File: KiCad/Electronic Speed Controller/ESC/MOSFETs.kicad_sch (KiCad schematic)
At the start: 0 parts

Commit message: Create MOSFETs driver schematic
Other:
- note added: "${TITLE}"
- title: (none) -> MOSFETs
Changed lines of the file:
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@@
 	(paper "A4")
 	(title_block
+		(title "MOSFETs")
 		(date "2025-01-09")
 		(rev "rev_1")
@@
 		(comment 4 "+212 643 241 400")
 	)
+	(text "${TITLE}"
+		(exclude_from_sim no)
+		(at 136.906 22.86 0)
+		(effects
+			(font
+				(face "Cascadia Mono NF")
+				(size 7.62 7.62)
+				(thickness 0.762)
+				(bold yes)
+			)
+			(justify top)
+		)
+	)
 )

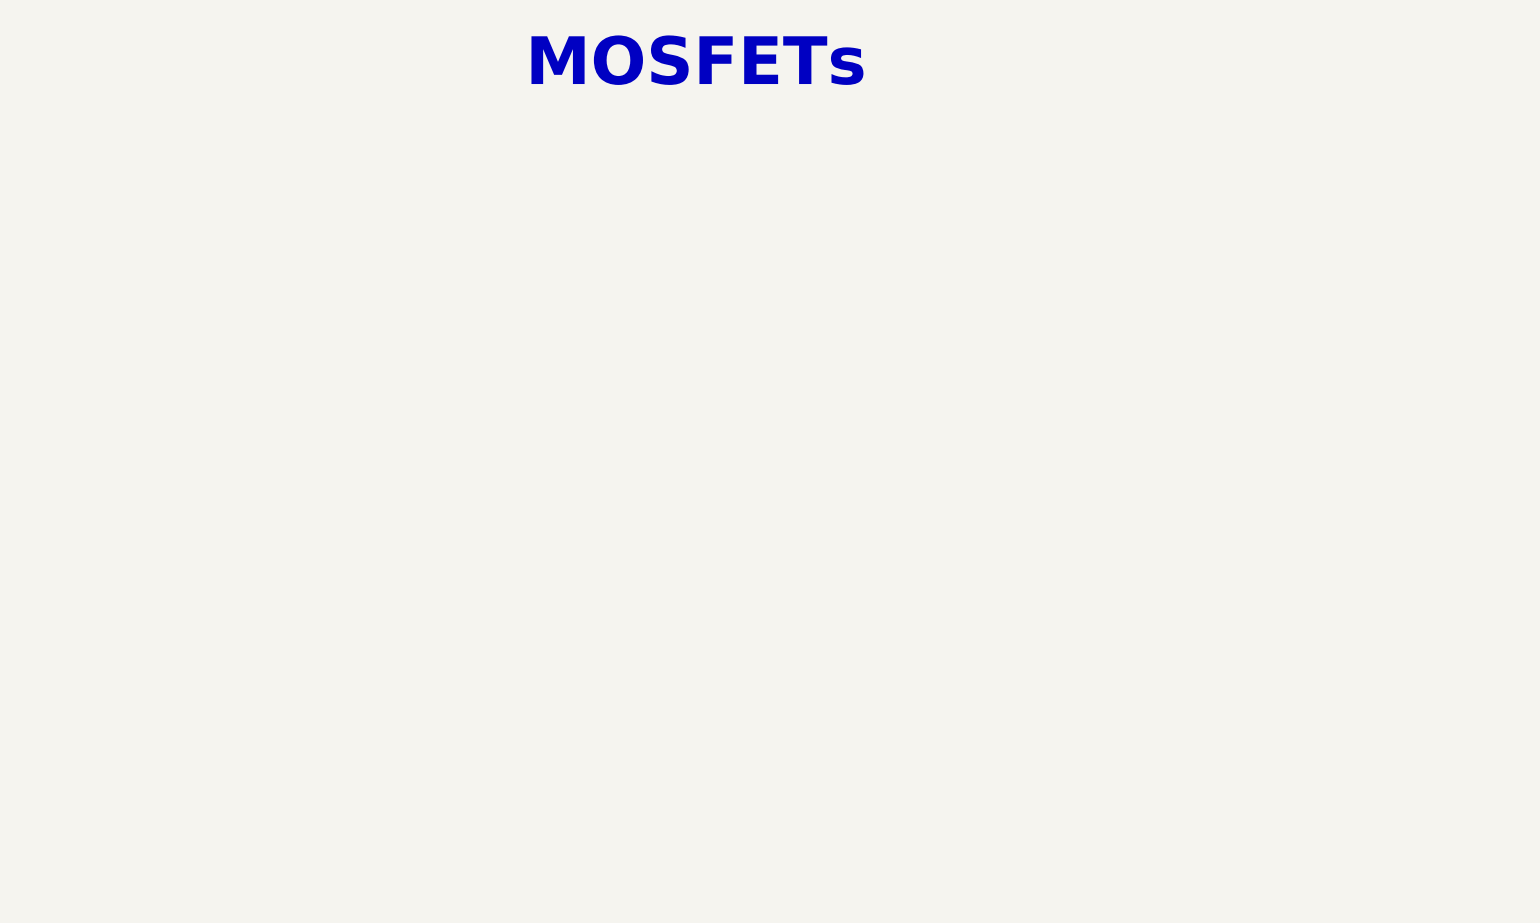
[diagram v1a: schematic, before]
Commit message: Create MOSFETs schematic (await ESC project)
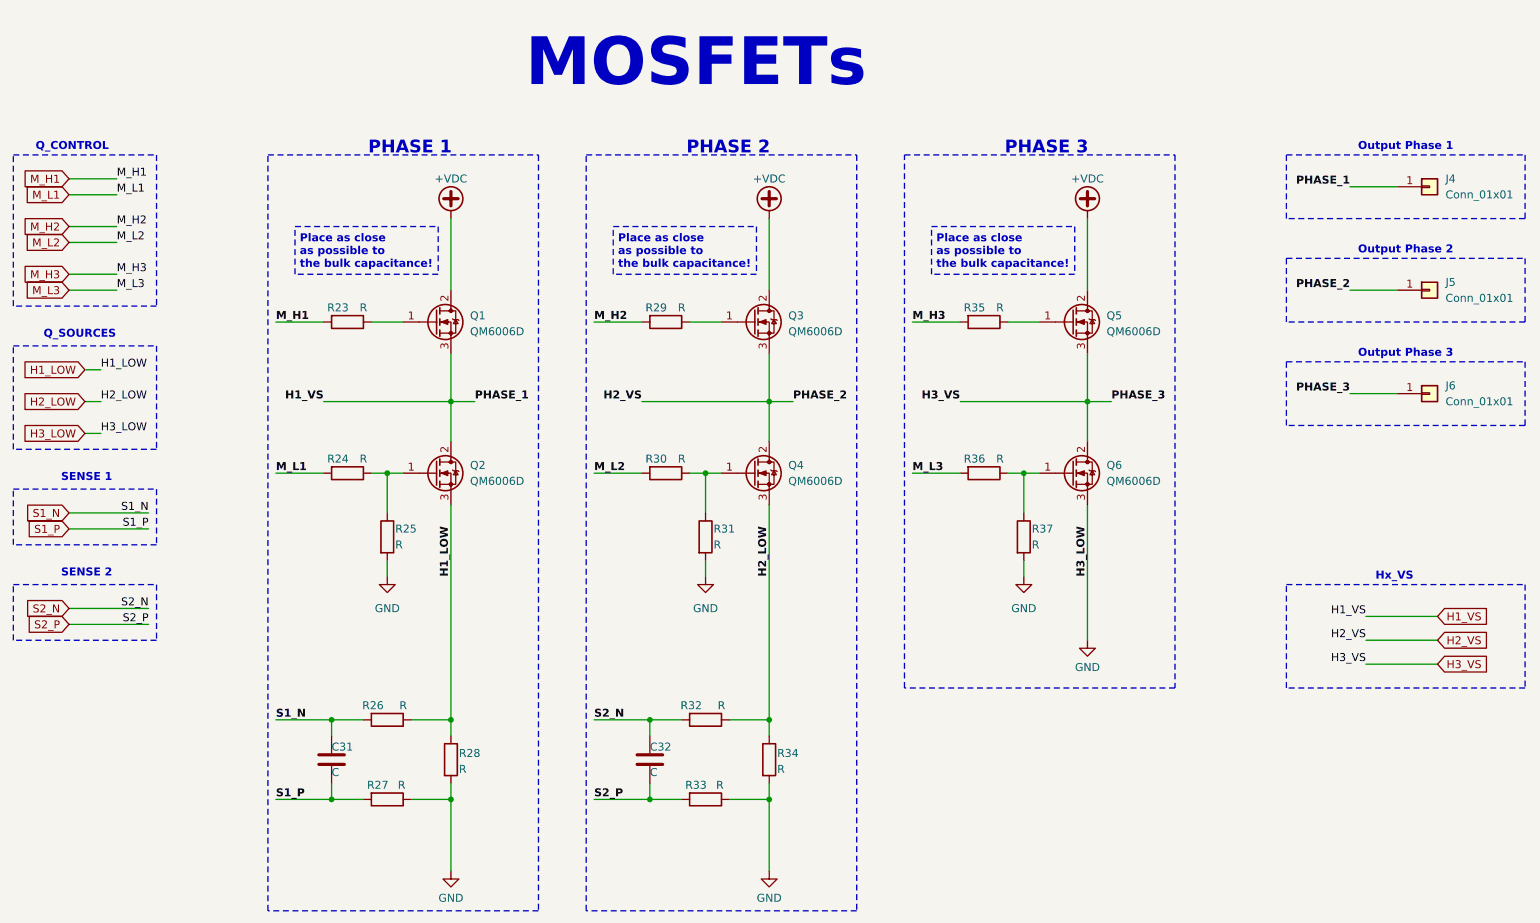
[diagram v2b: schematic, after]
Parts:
- added C31, C32: C, symbol Device:C
- added J4, J5, J6: Conn_01x01, symbol Connector_Generic:Conn_01x01
- added Q1, Q2, Q3, Q4, Q5, Q6: QM6006D, Package_TO_SOT_SMD:TO-252-2, symbol Transistor_FET:QM6006D
- added R23, R24, R25, R26, R27, R28, R29, R30, R31, R32, R33, R34, R35, R36, R37: R, symbol Device:R
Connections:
- new net: Q2.1 (G), R24.1, R25.1
- new net: Q4.1 (G), R30.1, R31.1
- new net: Q3.1 (G), R29.1
- new net: Q1.1 (G), R23.1
- new net: Q5.1 (G), R35.1
- new net: Q6.1 (G), R36.1, R37.1
- new net +VDC: Q1.2 (D), Q3.2 (D), Q5.2 (D)
- new net GND: Q6.3 (S), R25.2, R27.1, R28.2, R31.2, R33.1, R34.2, R37.2
- new net H1_LOW: Q2.3 (S), R26.1, R28.1
- new net H1_VS: J4.1 (Pin_1), Q1.3 (S), Q2.2 (D)
- new net H2_LOW: Q4.3 (S), R32.1, R34.1
- new net H2_VS: J5.1 (Pin_1), Q3.3 (S), Q4.2 (D)
- new net H3_VS: J6.1 (Pin_1), Q5.3 (S), Q6.2 (D)
- new net M_H1: R23.2
- new net M_H2: R29.2
- new net M_H3: R35.2
- new net M_L1: R24.2
- new net M_L2: R30.2
- new net M_L3: R36.2
- new net S1_N: C31.1, R26.2
- new net S1_P: C31.2, R27.2
- new net S2_N: C32.1, R32.2
- new net S2_P: C32.2, R33.2
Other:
- note added: "Hx_VS"
- note added: "Output Phase 1"
- note added: "Output Phase 2"
- note added: "Output Phase 3"
- note added: "PHASE 1"
- note added: "PHASE 2"
- note added: "PHASE 3"
- note added: "Place as close as possible to the bulk capacitance!"
- note added: "Q_CONTROL"
- note added: "Q_SOURCES"
- note added: "SENSE 1"
- note added: "SENSE 2"
